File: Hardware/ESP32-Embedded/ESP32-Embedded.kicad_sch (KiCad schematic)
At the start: 27 parts, among them J1 Micro USB, Q1 S8050, Q2 S8050, SW1 EN, SW2 BOOT, U1 ESP32-WROOM-32E, U2 AMS1117-3.3, U3 CH340G, Y1 12Mhz

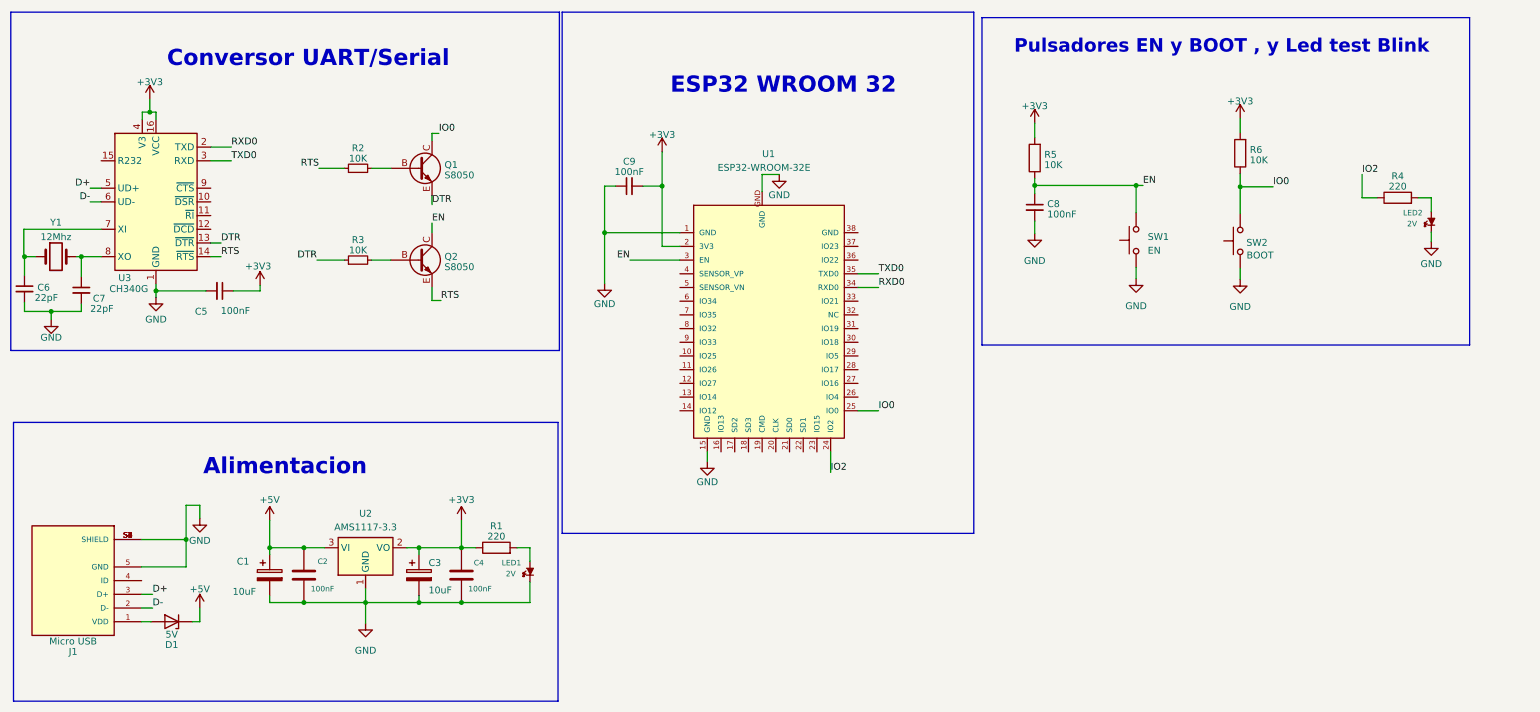
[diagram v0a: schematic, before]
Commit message: realice modificaciones importantes en sch para guia de eze y nueva placa para pcbway
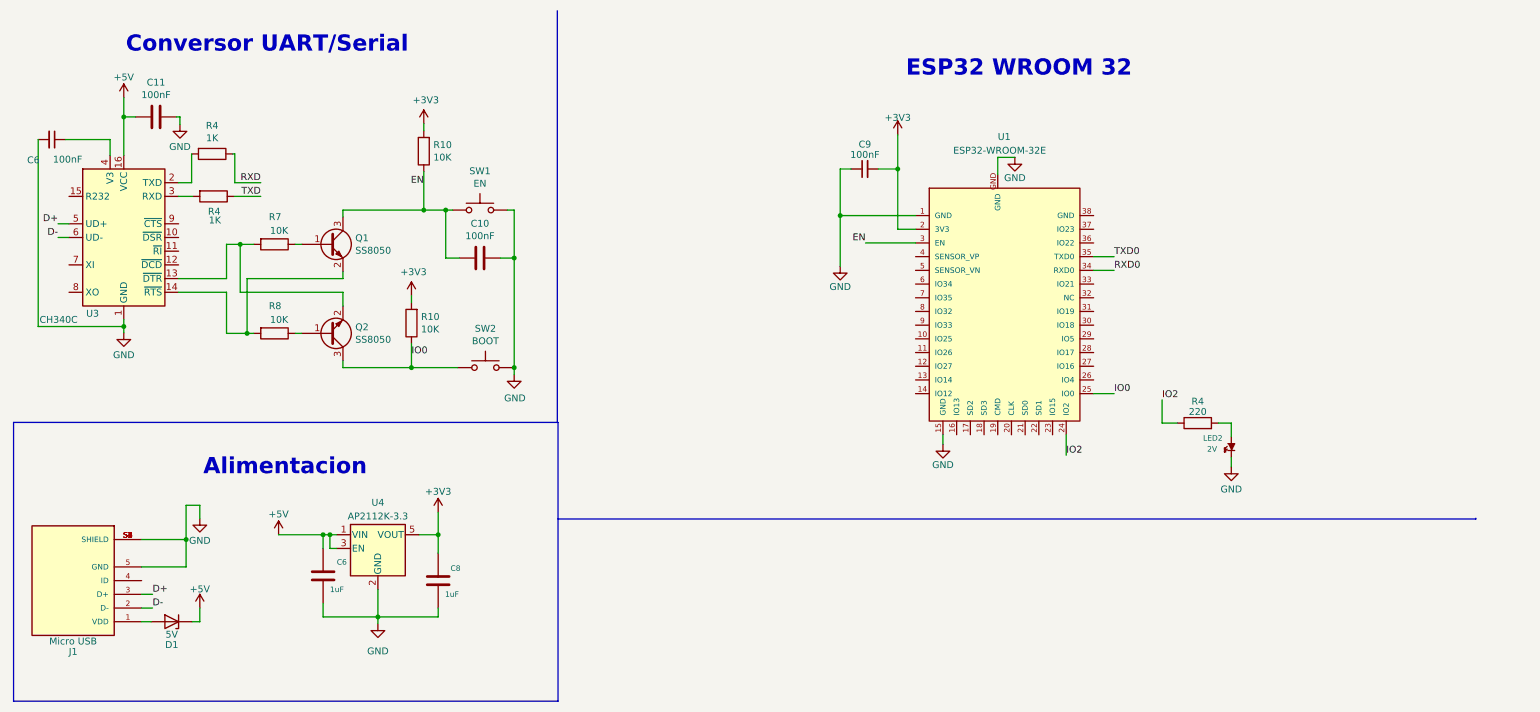
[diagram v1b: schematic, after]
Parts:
- removed C1, C3: 10uF, EESTN5:CAP_ELEC_SMD_4X5.5, symbol Device:C_Polarized
- removed C2, C4: 100nF, EESTN5:C_1206, symbol EESTN5:C
- removed C5, C8: 100nF, EESTN5:C_1206, symbol Device:C_Small
- removed C7: 22pF, EESTN5:C_1206, symbol Device:C_Small
- removed LED1: 2V, EESTN5:R_0805, symbol EESTN5:LED
- removed Q1, Q2: S8050, SS8050:SOT-23_BEC, symbol Transistor_BJT:S8050
- removed R1: 220, EESTN5:R_1206, symbol Device:R
- removed R2, R3: 10K, EESTN5:R_1206, symbol Device:R_Small
- removed R5, R6: 10K, EESTN5:R_1206, symbol Device:R
- removed SW1: EN, Button_Switch_SMD:SW_SPST_B3U-1000P-B, symbol EESTN5:SW_Push
- removed SW2: BOOT, Button_Switch_SMD:SW_SPST_B3U-1000P-B, symbol EESTN5:SW_Push
- removed U2: AMS1117-3.3, Package_TO_SOT_SMD:SOT-223-3_TabPin2, symbol Regulator_Linear:AMS1117-3.3
- removed Y1: 12Mhz, Crystal:Crystal_SMD_3215-2Pin_3.2x1.5mm, symbol Device:Crystal
- added C10, C11: 100nF, Capacitor_SMD:C_0402_1005Metric, symbol Device:C
- added C6, C8: 1uF, EESTN5:C_0805, symbol EESTN5:C
- added Q1, Q2: SS8050, Package_TO_SOT_SMD:SOT-23, symbol Transistor_BJT:MMBT3904
- added R10 (x2), R7, R8: 10K, Resistor_SMD:R_0402_1005Metric, symbol Device:R
- added R4 (x2): 1K, Resistor_SMD:R_0402_1005Metric, symbol Device:R
- added SW1: EN, Button_Switch_SMD:SW_Push_SPST_NO_Alps_SKRK, symbol Switch:SW_Push
- added SW2: BOOT, Button_Switch_SMD:SW_Push_SPST_NO_Alps_SKRK, symbol Switch:SW_Push
- added U4: AP2112K-3.3, Package_TO_SOT_SMD:SOT-23-5, symbol Regulator_Linear:AP2112K-3.3
- C6: value 22pF -> 100nF
- U3: value CH340G -> CH340C
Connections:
- net +3V3: now also C8.1, R10.2, R10.2, U4.5 (VOUT); no longer U3.16 (VCC), U3.4 (V3)
- net +5V: now also U3.16 (VCC), C11.2, C6.1, U4.1 (VIN), U4.3 (EN)
- net EN: now also C10.2, Q1.3 (C), R10.1, SW1.1
- net GND: now also C10.1, C11.1, C6.2, C8.2, SW1.2, SW2.2, U4.2 (GND)
- net IO0: now also Q2.3 (C), R10.1, SW2.1
- net RXD0: no longer U3.2 (TXD)
- net TXD0: no longer U3.3 (RXD)
- net at C6.1: now also U3.4 (V3); no longer U3.7 (XI)
- net DTR: no longer names the net of U3.13 (~{DTR})
- net DTR: now also Q2.2 (E), R7.2
- net RTS: no longer names the net of U3.14 (~{RTS})
- net RTS: now also Q1.2 (E), R8.2
- new net: R4.2, U3.3 (RXD)
- new net: Q1.1 (B), R7.1
- new net: Q2.1 (B), R8.1
- new net: R4.2, U3.2 (TXD)
- new net RXD: R4.1
- new net TXD: R4.1
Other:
- note removed: "Pulsadores EN y BOOT , y Led test Blink"
- moved on the sheet: C9, LED2, R4, U1, U3
